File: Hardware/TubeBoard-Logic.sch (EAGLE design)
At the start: 23 parts, among them IC1 74HC373DW, IC2 74HC373DW, IC3 74HC85D, IC4 74HC08D, IC5 74HC04D

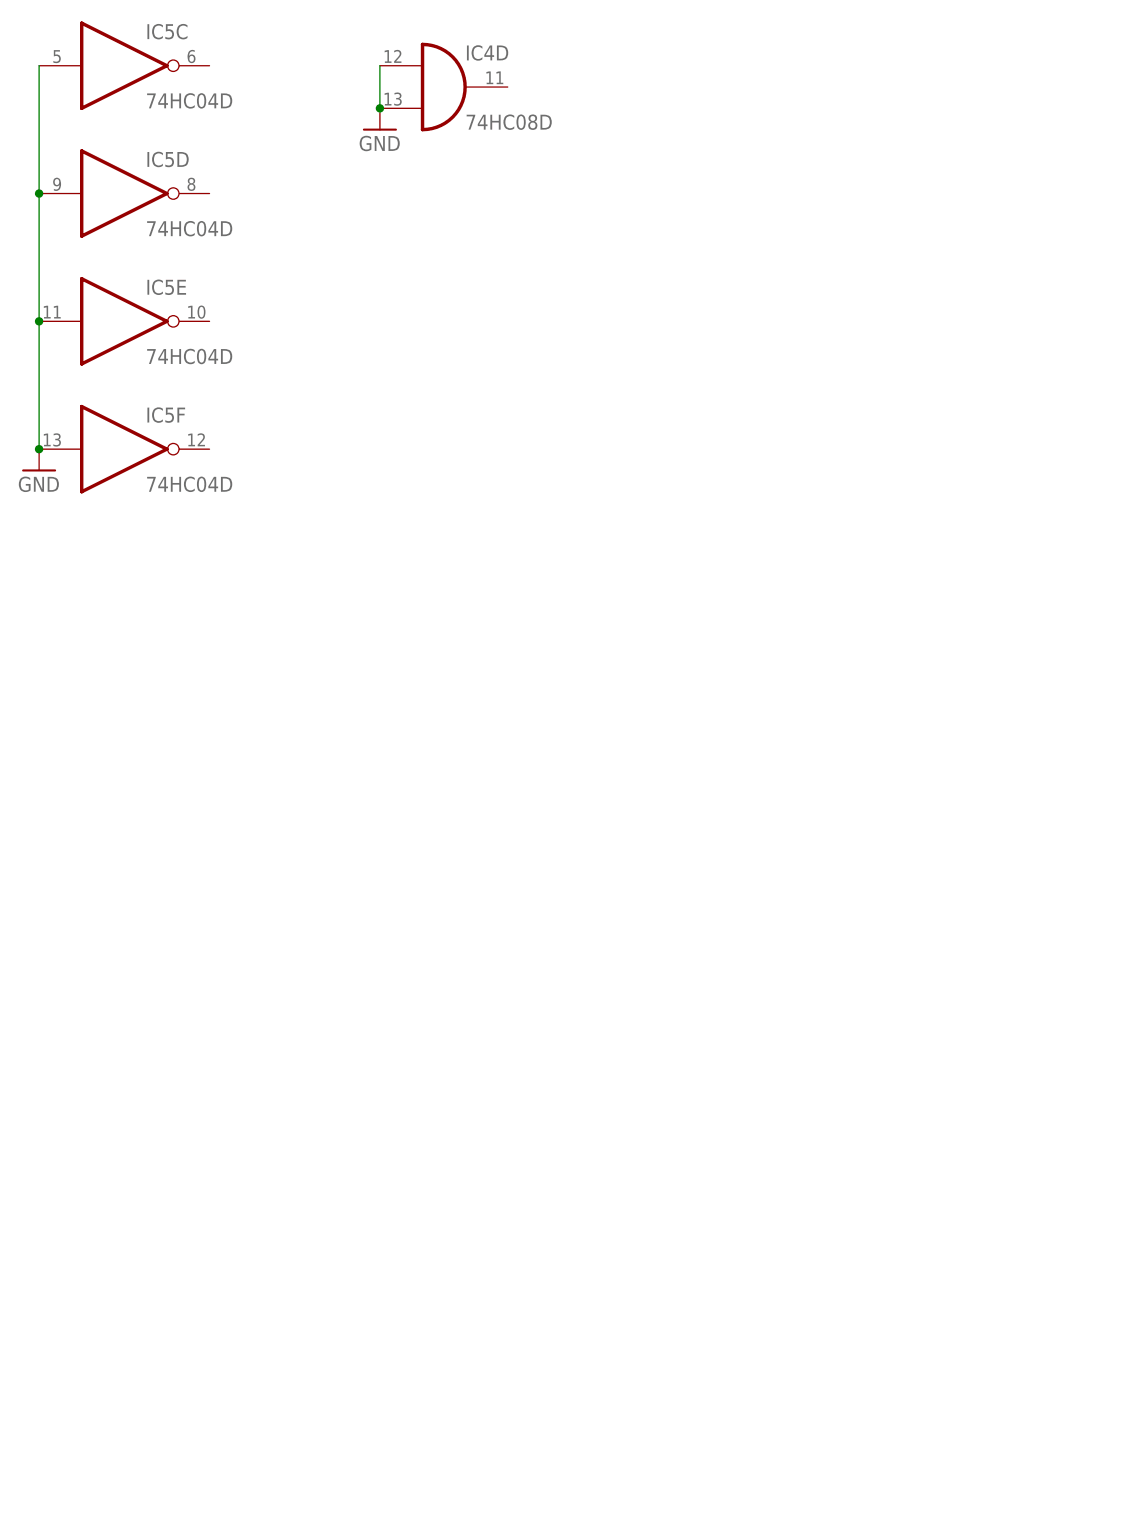
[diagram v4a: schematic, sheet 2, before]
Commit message: added ARM chip to driver boards to PWM tubes
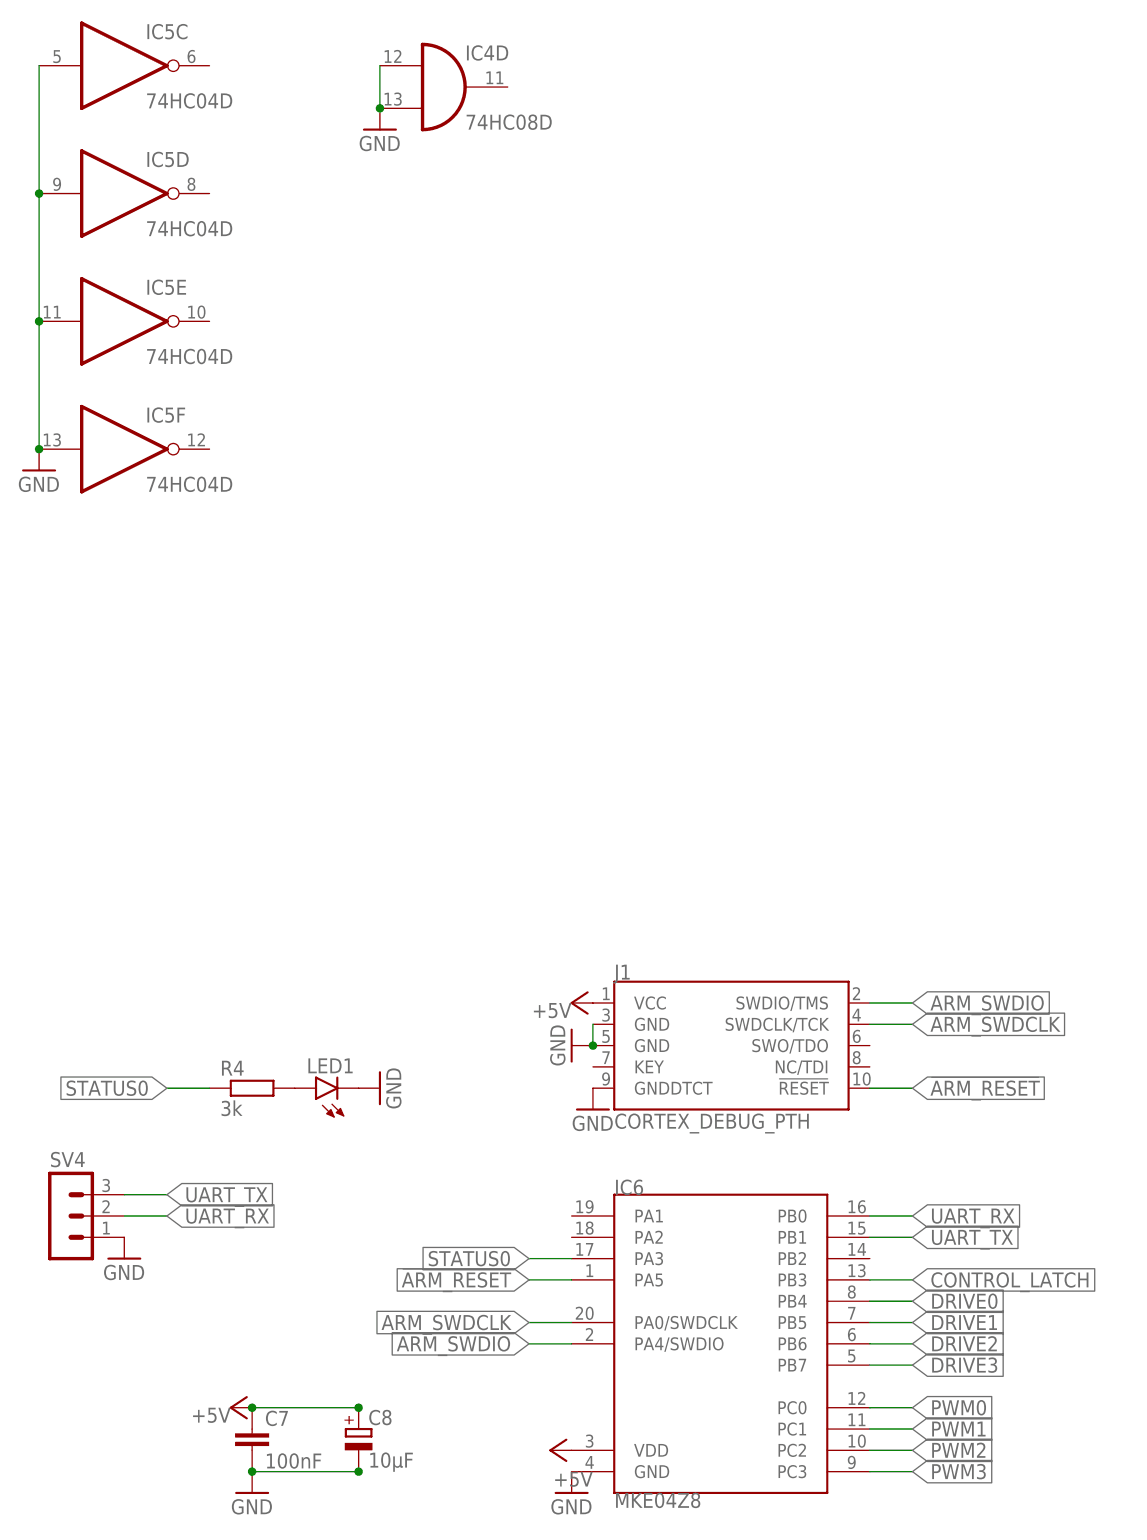
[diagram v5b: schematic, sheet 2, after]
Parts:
- added C7: 100nF, rcl:C-EUC1206
- added C8: 10µF, rcl:CPOL-EUSMCB
- added IC6: MKE04Z8, Parts:MKE04Z8SOIC20
- added J1: CORTEX_DEBUG_PTH, SparkFun-Connectors:CORTEX_DEBUG_PTH
- added LED1: (no value), led:LEDCHIPLED_1206
- added R4: 3k, rcl:R-EU_R2012
- added SV4: (no value), con-lstb:MA03-1
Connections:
- removed net DRIVE_HI: IC2A.8Q, SV1.3
- removed net DRIVE_LO: IC2A.6Q, SV1.7
- removed net DRIVE_MED: IC2A.7Q, SV1.5
- new net !ARM_RESET: IC6.PA5, J1.!RESET
- new net ARM_SWDCLK: IC6.PA0/SWDCLK, J1.SWDCLK/TCK
- new net ARM_SWDIO: IC6.PA4/SWDIO, J1.SWDIO/TMS
- new net DRIVE0: IC2A.5Q, IC6.PB4
- new net DRIVE1: IC2A.6Q, IC6.PB5
- new net DRIVE2: IC2A.7Q, IC6.PB6
- new net DRIVE3: IC2A.8Q, IC6.PB7
- new net N$9: LED1.A, R4.2
- new net PWM0: IC6.PC0, SV1.7
- new net PWM1: IC6.PC1, SV1.5
- new net PWM2: IC6.PC2, SV1.3
- new net PWM3: IC6.PC3, SV1.4
- new net STATUS0: IC6.PA3, R4.1
- new net UART_RX: IC6.PB0, SV4.2
- new net UART_TX: IC6.PB1, SV4.3
- net +5V: now also C7.1, C8.+, IC6.VDD, J1.VCC
- net CONTROL_LATCH: now also IC6.PB3
- net GND: now also C7.2, C8.-, IC6.GND, J1.GND@3, J1.GND@5, J1.GNDDTCT, LED1.C, SV4.1; no longer SV1.4

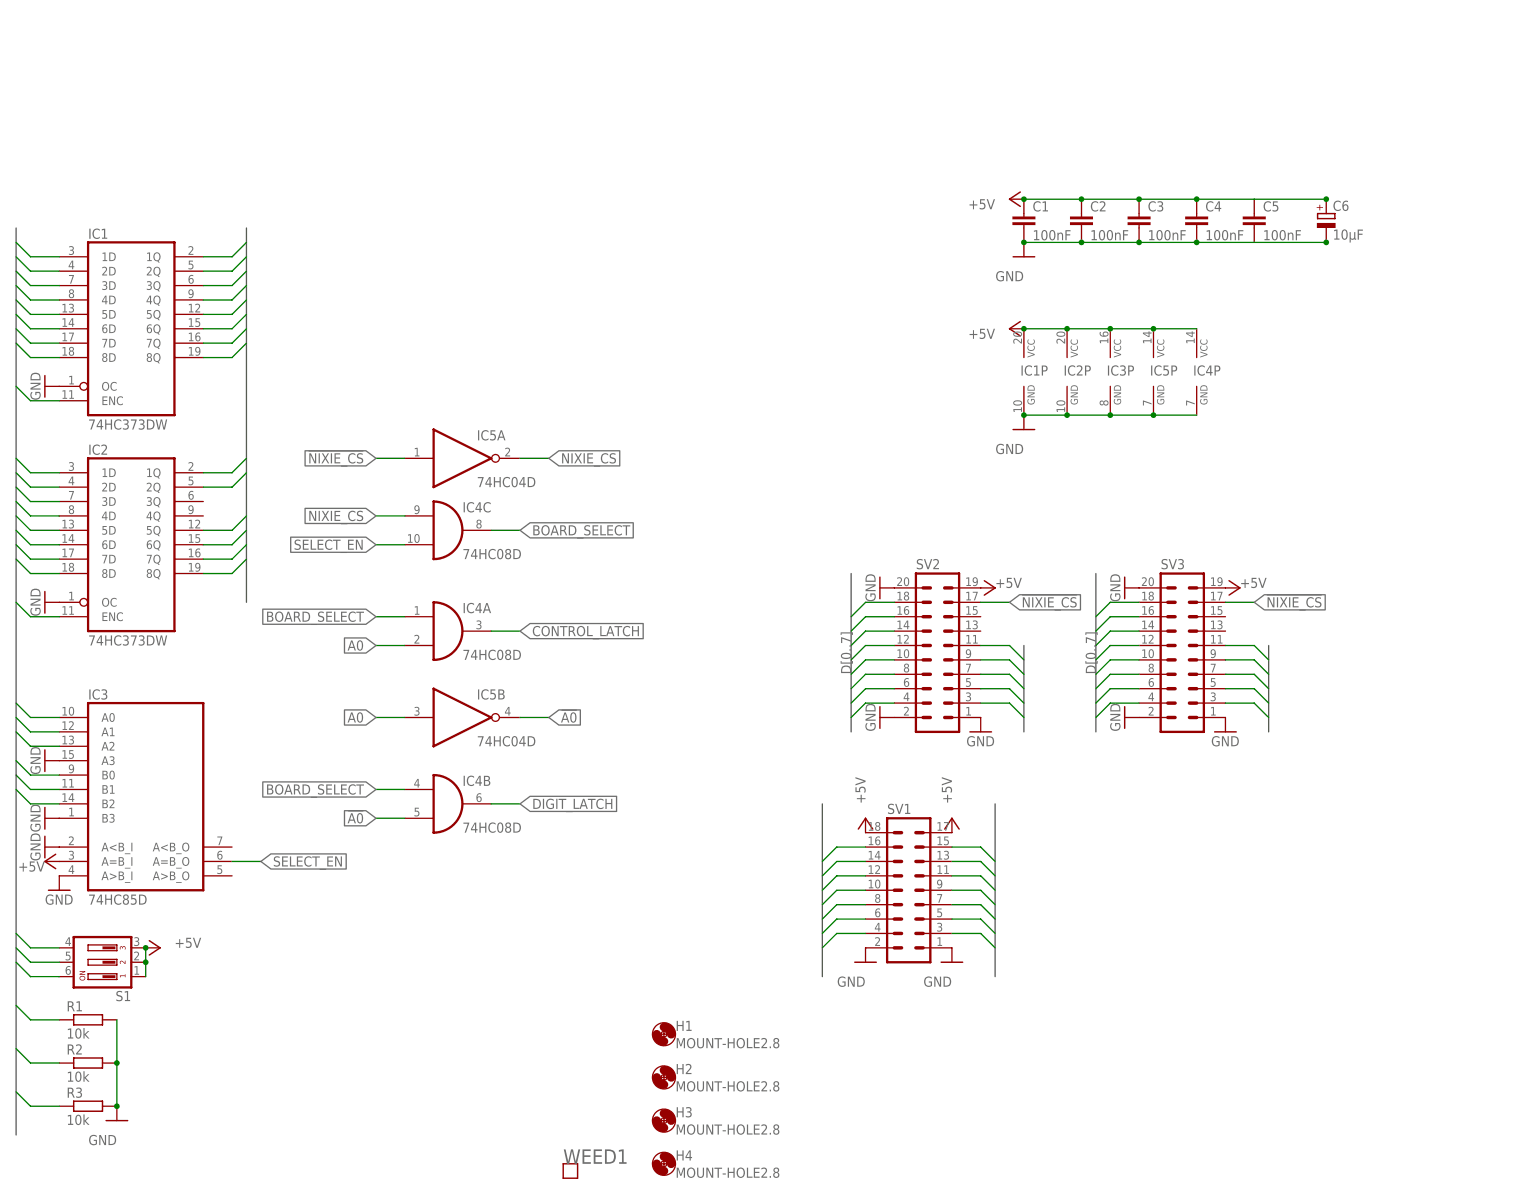
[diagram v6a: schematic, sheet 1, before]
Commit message: more work for vfd command handling
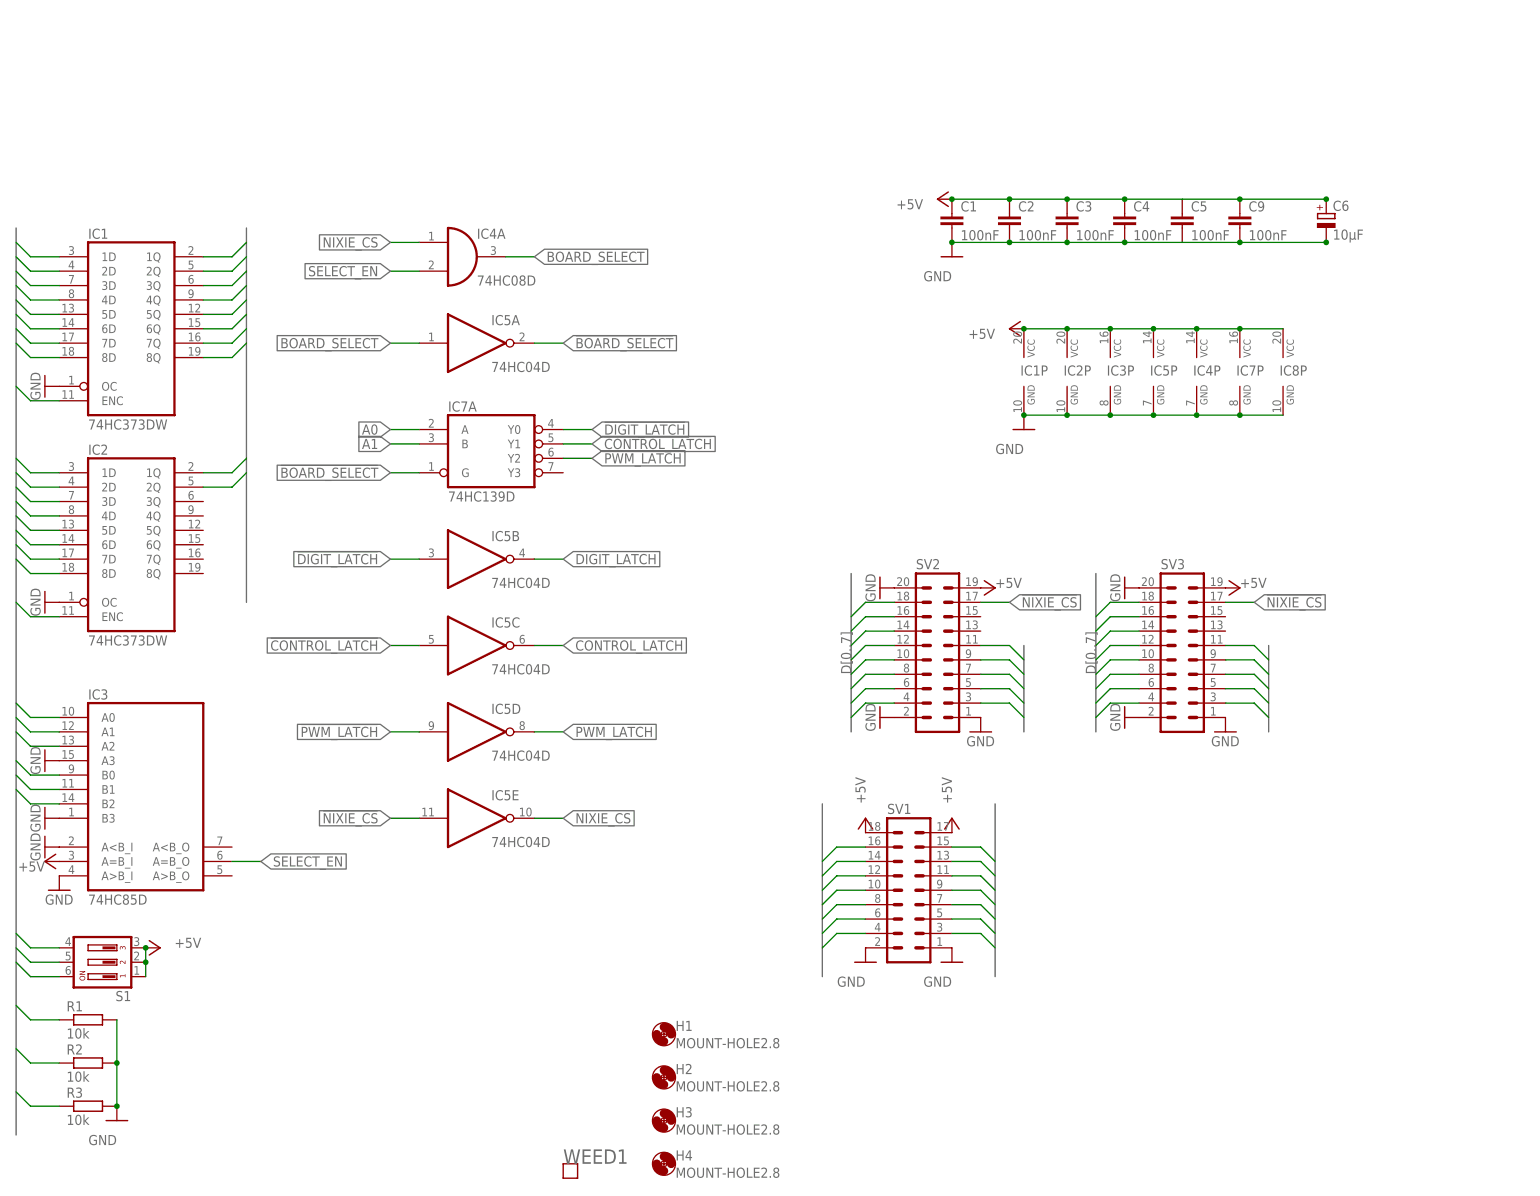
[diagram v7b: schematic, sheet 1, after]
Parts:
- added C9: 100nF, rcl:C-EUC1206
- added IC7: 74HC139D, 74xx-eu:74HC139D
- added IC8: 74HC373DW, 74xx-eu:74HC373DW
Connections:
- removed net !A0: IC4B.I1, IC5B.O
- removed net DRIVE0: IC2A.5Q, IC6.PB4
- removed net DRIVE1: IC2A.6Q, IC6.PB5
- removed net DRIVE2: IC2A.7Q, IC6.PB6
- removed net DRIVE3: IC2A.8Q, IC6.PB7
- new net !BOARD_SELECT: IC5A.O, IC7A.G
- new net !CONTROL_LATCH: IC5C.I, IC7A.Y1
- new net !DIGIT_LATCH: IC5B.I, IC7A.Y0
- new net !PWM_LATCH: IC5D.I, IC7A.Y2
- new net PWM_D0: IC6.PB4, IC8A.1Q
- new net PWM_D1: IC6.PB5, IC8A.2Q
- new net PWM_D2: IC6.PB6, IC8A.3Q
- new net PWM_D3: IC6.PB7, IC8A.4Q
- new net PWM_LATCH: IC5D.O, IC6.PB3, IC8A.ENC
- net !NIXIE_CS: now also IC5E.I; no longer IC5A.I
- net +5V: now also C9.1, IC7P.VCC, IC8P.VCC
- net A0: now also IC7A.A; no longer IC4A.I1, IC5B.I
- net A1: now also IC7A.B
- net BOARD_SELECT: now also IC4A.O, IC5A.I; no longer IC4A.I0, IC4B.I0, IC4C.O
- net CONTROL_LATCH: now also IC5C.O; no longer IC4A.O, IC6.PB3
- net D0: now also IC8A.1D
- net D1: now also IC8A.2D
- net D2: now also IC8A.3D
- net D3: now also IC8A.4D
- net D4: now also IC8A.5D
- net D5: now also IC8A.6D
- net D6: now also IC8A.7D
- net D7: now also IC8A.8D
- net DIGIT_LATCH: now also IC5B.O; no longer IC4B.O
- net GND: now also C9.2, IC4B.I0, IC4B.I1, IC4C.I0, IC4C.I1, IC7P.GND, IC8A.OC, IC8P.GND; no longer IC5C.I, IC5D.I, IC5E.I
- net NIXIE_CS: now also IC4A.I0, IC5E.O; no longer IC4C.I0, IC5A.O
- net SELECT_EN: now also IC4A.I1; no longer IC4C.I1
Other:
- moved on the sheet: C1, C2, C3, C4, C5, IC4A, IC4D, IC5A, IC5B, IC5F
